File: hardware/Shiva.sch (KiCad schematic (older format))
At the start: 101 parts, among them J1 JACK_FEMALE_STEREO, J2 JACK_FEMALE_STEREO, J3 JACK_FEMALE_STEREO, J4 JACK_FEMALE_STEREO, J5 JACK_FEMALE_STEREO, J6 JACK_FEMALE_STEREO, J7 JACK_FEMALE_STEREO, J8 JACK_FEMALE_STEREO, P1 DIN_5, U1 LTC6242, U2 LTC6242, U3 LD1117S33CTR

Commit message: Fix labels for connections to new LEDs
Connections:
- net CHANNEL_01_SW: no longer Q?.2 (G), Q?.2 (G), Q?.2 (G), Q?.2 (G), Q?.2 (G), Q?.2 (G), Q?.2 (G), R?.1, R?.1, R?.1, R?.1, R?.1, R?.1, R?.1
- net DETECT_01: no longer R?.2, R?.2, R?.2, R?.2, R?.2, R?.2, R?.2
- net DETECT_02: now also R?.2; no longer J2.SS
- net DETECT_03: now also R?.2; no longer J3.SS
- net DETECT_04: now also R?.2; no longer J1.SS
- net DETECT_05: now also R?.2; no longer J5.SS
- net DETECT_06: now also R?.2; no longer J6.SS
- net DETECT_07: now also R?.2; no longer J7.SS
- net DETECT_08: now also R?.2; no longer J8.SS
- new net CHANNEL_02_SW: J2.SS, Q?.2 (G), R?.1
- new net CHANNEL_03_SW: J3.SS, Q?.2 (G), R?.1
- new net CHANNEL_04_SW: J1.SS, Q?.2 (G), R?.1
- new net CHANNEL_05_SW: J5.SS, Q?.2 (G), R?.1
- new net CHANNEL_06_SW: J6.SS, Q?.2 (G), R?.1
- new net CHANNEL_07_SW: J7.SS, Q?.2 (G), R?.1
- new net CHANNEL_08_SW: J8.SS, Q?.2 (G), R?.1
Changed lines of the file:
@@
 NoConn ~ 2200 3900
 NoConn ~ 2200 3800
-Text Label 2700 4300 2    60   ~ 0
-DETECT_02
 Wire Wire Line
 	3000 4050 3000 4200
@@
 NoConn ~ 2200 4000
 Wire Wire Line
-	2200 4300 2700 4300
+	2200 4300 2950 4300
 $Comp
 L R R6
@@
 NoConn ~ 2200 6000
 NoConn ~ 2200 5900
-Text Label 2700 6400 2    60   ~ 0
-DETECT_03
 Wire Wire Line
 	3000 6150 3000 6300
@@
 NoConn ~ 2200 6100
 Wire Wire Line
-	2200 6400 2700 6400
+	2200 6400 2950 6400
 $Comp
 L R R7
@@
 NoConn ~ 2150 8050
 NoConn ~ 2150 7950
-Text Label 2650 8450 2    60   ~ 0
+Text Label 11900 8100 0    60   ~ 0
 DETECT_04
 Wire Wire Line
@@
 NoConn ~ 2150 8150
 Wire Wire Line
-	2150 8450 2650 8450
+	2150 8450 2900 8450
 $Comp
 L R R5
@@
 NoConn ~ 7350 1800
 NoConn ~ 7350 1700
-Text Label 7850 2200 2    60   ~ 0
+Text Label 13750 4650 0    60   ~ 0
 DETECT_05
 Wire Wire Line
@@
 NoConn ~ 7350 1900
 Wire Wire Line
-	7350 2200 7850 2200
+	7350 2200 8100 2200
 $Comp
 L R R20
@@
 NoConn ~ 7300 3850
 NoConn ~ 7300 3750
-Text Label 7800 4250 2    60   ~ 0
+Text Label 13750 5800 0    60   ~ 0
 DETECT_06
 Wire Wire Line
@@
 NoConn ~ 7300 3950
 Wire Wire Line
-	7300 4250 7800 4250
+	7300 4250 8050 4250
 $Comp
 L R R18
@@
 NoConn ~ 7300 5950
 NoConn ~ 7300 5850
-Text Label 7800 6350 2    60   ~ 0
+Text Label 13850 7000 0    60   ~ 0
 DETECT_07
 Wire Wire Line
@@
 NoConn ~ 7300 6050
 Wire Wire Line
-	7300 6350 7800 6350
+	7300 6350 8050 6350
 $Comp
 L R R19
@@
 NoConn ~ 7250 8000
 NoConn ~ 7250 7900
-Text Label 7750 8400 2    60   ~ 0
+Text Label 13850 8150 0    60   ~ 0
 DETECT_08
 Wire Wire Line
@@
 NoConn ~ 7250 8100
 Wire Wire Line
-	7250 8400 7750 8400
+	7250 8400 8000 8400
 $Comp
 L R R17
@@
 	13000 4200 12950 4200
 Text Label 11800 5750 0    60   ~ 0
-DETECT_01
+DETECT_02
 $Comp
 L VCC #PWR?
@@
 	12650 6050 11850 6050
 Connection ~ 12650 5750
-Text Label 11850 6050 0    60   ~ 0
-CHANNEL_01_SW
 Wire Wire Line
 	12200 5350 12200 5200
 Wire Wire Line
 	13000 5350 12950 5350
-Text Label 13750 4650 0    60   ~ 0
-DETECT_01
 $Comp
 L VCC #PWR?
@@
 	14600 4950 13800 4950
 Connection ~ 14600 4650
-Text Label 13800 4950 0    60   ~ 0
-CHANNEL_01_SW
 Wire Wire Line
 	14150 4250 14150 4100
 Wire Wire Line
 	14950 4250 14900 4250
-Text Label 13750 5800 0    60   ~ 0
-DETECT_01
 $Comp
 L VCC #PWR?
@@
 	14600 6100 13800 6100
 Connection ~ 14600 5800
-Text Label 13800 6100 0    60   ~ 0
-CHANNEL_01_SW
 Wire Wire Line
 	14150 5400 14150 5250
@@
 	14950 5400 14900 5400
 Text Label 11900 6950 0    60   ~ 0
-DETECT_01
+DETECT_03
 $Comp
 L VCC #PWR?
@@
 	12750 7250 11950 7250
 Connection ~ 12750 6950
-Text Label 11950 7250 0    60   ~ 0
-CHANNEL_01_SW
 Wire Wire Line
 	12300 6550 12300 6400
 Wire Wire Line
 	13100 6550 13050 6550
-Text Label 11900 8100 0    60   ~ 0
-DETECT_01
 $Comp
 L VCC #PWR?
@@
 	12750 8400 11950 8400
 Connection ~ 12750 8100
-Text Label 11950 8400 0    60   ~ 0
-CHANNEL_01_SW
 Wire Wire Line
 	12300 7700 12300 7550
 Wire Wire Line
 	13100 7700 13050 7700
-Text Label 13850 7000 0    60   ~ 0
-DETECT_01
 $Comp
 L VCC #PWR?
@@
 	14700 7300 13900 7300
 Connection ~ 14700 7000
-Text Label 13900 7300 0    60   ~ 0
-CHANNEL_01_SW
 Wire Wire Line
 	14250 6600 14250 6450
 Wire Wire Line
 	15050 6600 15000 6600
-Text Label 13850 8150 0    60   ~ 0
-DETECT_01
 $Comp
 L VCC #PWR?
@@
 	14700 8450 13900 8450
 Connection ~ 14700 8150
+Wire Wire Line
+	14250 7750 14250 7600
+Wire Wire Line
+	15050 7750 15000 7750
+Text Label 2950 4300 2    60   ~ 0
+CHANNEL_02_SW
+Text Label 2900 8450 2    60   ~ 0
+CHANNEL_04_SW
+Text Label 8100 2200 2    60   ~ 0
+CHANNEL_05_SW
+Text Label 8050 4250 2    60   ~ 0
+CHANNEL_06_SW
+Text Label 8050 6350 2    60   ~ 0
+CHANNEL_07_SW
+Text Label 8000 8400 2    60   ~ 0
+CHANNEL_08_SW
+Text Label 2950 6400 2    60   ~ 0
+CHANNEL_03_SW
+Text Label 13900 7300 0    60   ~ 0
+CHANNEL_07_SW
 Text Label 13900 8450 0    60   ~ 0
-CHANNEL_01_SW
-Wire Wire Line
-	14250 7750 14250 7600
-Wire Wire Line
-	15050 7750 15000 7750
+CHANNEL_08_SW
+Text Label 13800 6100 0    60   ~ 0
+CHANNEL_06_SW
+Text Label 13800 4950 0    60   ~ 0
+CHANNEL_05_SW
+Text Label 11850 6050 0    60   ~ 0
+CHANNEL_02_SW
+Text Label 11950 7250 0    60   ~ 0
+CHANNEL_03_SW
+Text Label 11950 8400 0    60   ~ 0
+CHANNEL_04_SW
 $EndSCHEMATC

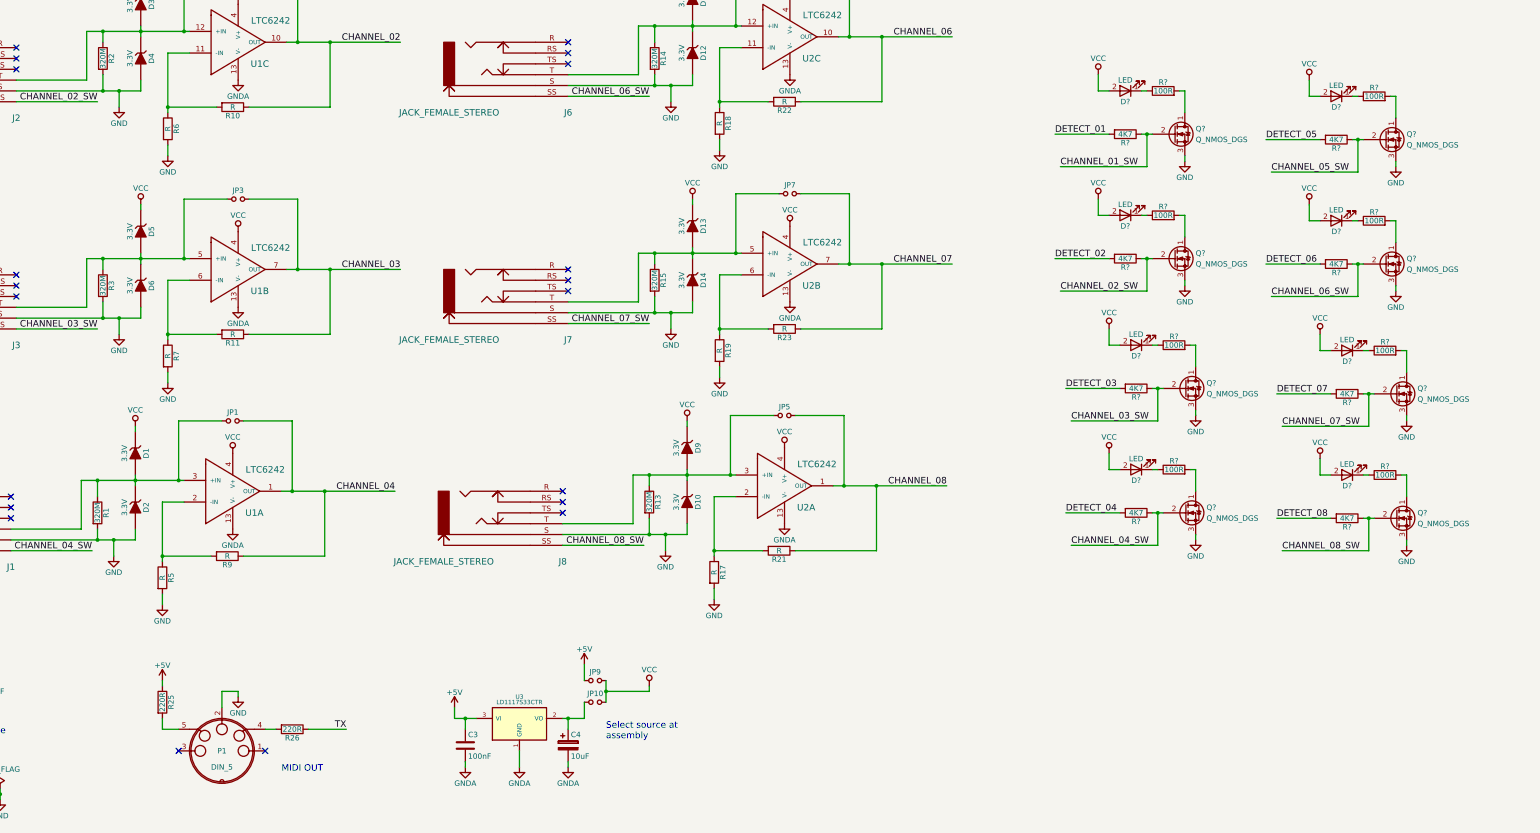
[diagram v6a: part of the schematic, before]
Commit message: Assign footprints for new LED-related components
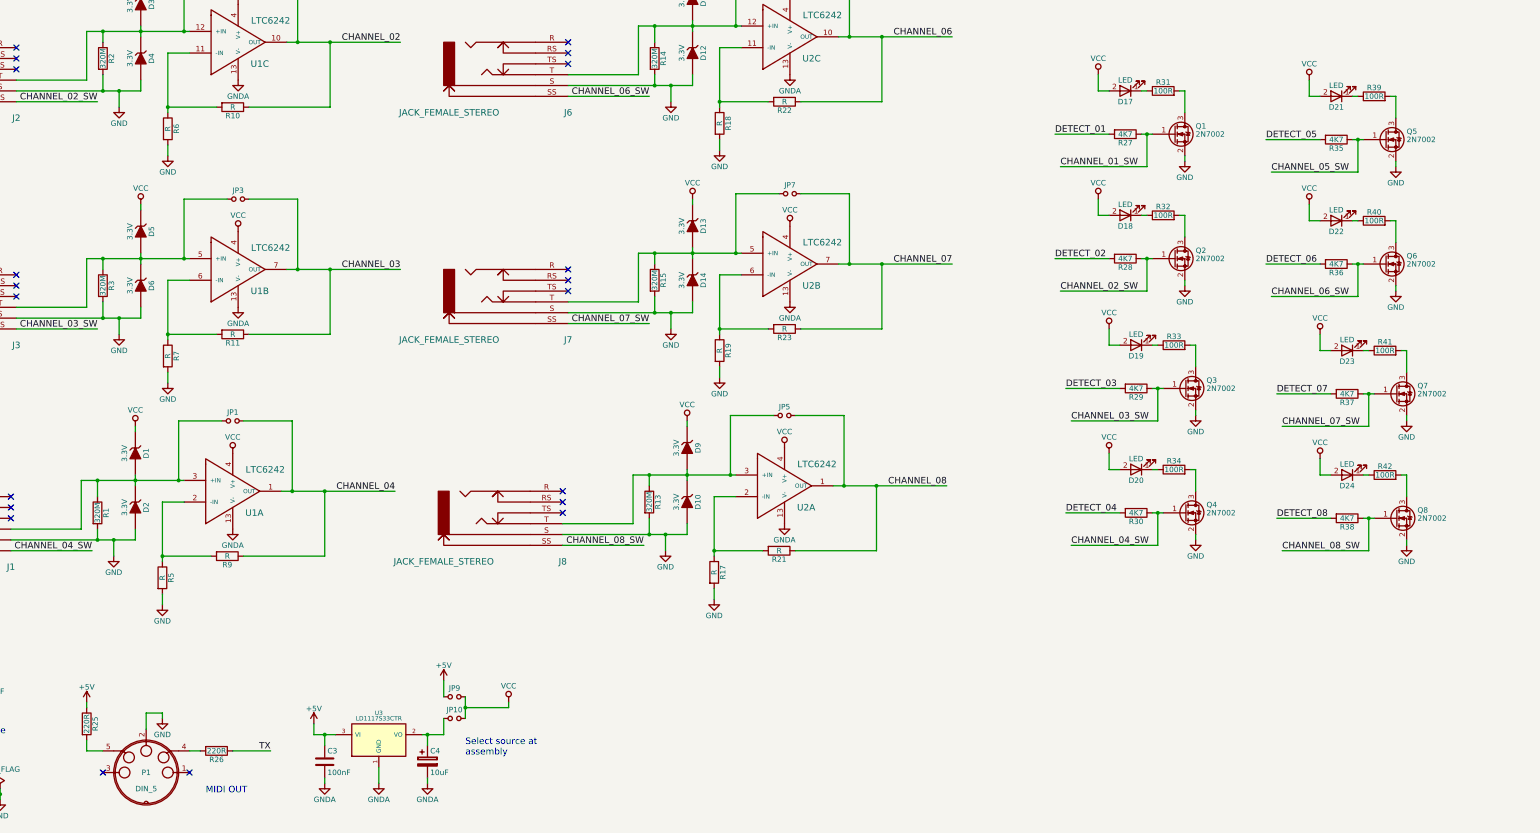
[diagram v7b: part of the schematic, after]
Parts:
- removed Q? (x8): Q_NMOS_DGS, symbol Q_NMOS_DGS
- added Q1, Q2, Q3, Q4, Q5, Q6, Q7, Q8: 2N7002, TO_SOT_Packages_SMD:SOT-23_Handsoldering, symbol 2N7002
- D17, D18, D19, D20, D21, D22, D23, D24: renamed from D?; footprint (none) -> LEDs:LED_0805_HandSoldering
- R10, R11, R12, R17, R18, R19, R20, R21, R22, R23, R24, R25, R26, R5, R6, R7, R8, R9: footprint Resistors_SMD:R_0603_HandSoldering -> Resistors_SMD:R_0805_HandSoldering
- R27, R28, R29, R30, R31, R32, R33, R34, R35, R36, R37, R38, R39, R40, R41, R42: renamed from R?; footprint Resistors_SMD:R_0603_HandSoldering -> Resistors_SMD:R_0805_HandSoldering
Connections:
- net CHANNEL_01_SW: now also Q1.1 (G)
- net CHANNEL_02_SW: now also Q2.1 (G)
- net CHANNEL_03_SW: now also Q3.1 (G)
- net CHANNEL_04_SW: now also Q4.1 (G)
- net CHANNEL_05_SW: now also Q5.1 (G)
- net CHANNEL_06_SW: now also Q6.1 (G)
- net CHANNEL_07_SW: now also Q7.1 (G)
- net CHANNEL_08_SW: now also Q8.1 (G)
- net GND: now also Q1.2 (S), Q2.2 (S), Q3.2 (S), Q4.2 (S), Q5.2 (S), Q6.2 (S), Q7.2 (S), Q8.2 (S)
- net at R31.2: now also Q1.3 (D)
- net at R32.2: now also Q2.3 (D)
- net at R39.2: now also Q5.3 (D)
- net at R40.2: now also Q6.3 (D)
- net at R33.2: now also Q3.3 (D)
- net at R34.2: now also Q4.3 (D)
- net at R41.2: now also Q7.3 (D)
- net at R42.2: now also Q8.3 (D)
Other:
- moved on the sheet: C3, C4, JP10, JP9, P1, R25, R26, U3
